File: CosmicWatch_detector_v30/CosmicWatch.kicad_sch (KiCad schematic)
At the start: 86 parts, among them J3 RJ45, P1 CONN_01X04, P10 CONN_02X02, P11 CONN_01X01, P12 CONN_01X01, P13 CONN_01X01, P14 CONN_01X01, P15 CONN_02X04, P16 CONN_01X02, P19 CONN_01X01, P2 CONN_01X01, P3 CONN_01X04, P4 CONN_01X04, P5 CONN_01X02, P7 CONN_01X01, P8 CONN_01X01, Q2 2N7002, SW1 RESET, U1 MAX5026, U13 TS5A1066, U16 UMCC, U17 UMCC, U2 SiPM_MicroFJ−300XX−TSV, U22 UMCC, U23 UMCC, U3 MMCX, U4 TS5A1066, U5 LMH6658, U5 RasberryPi_Pico, U6 LMH6658, U7 TPS6040X, U8 sd_card_socket

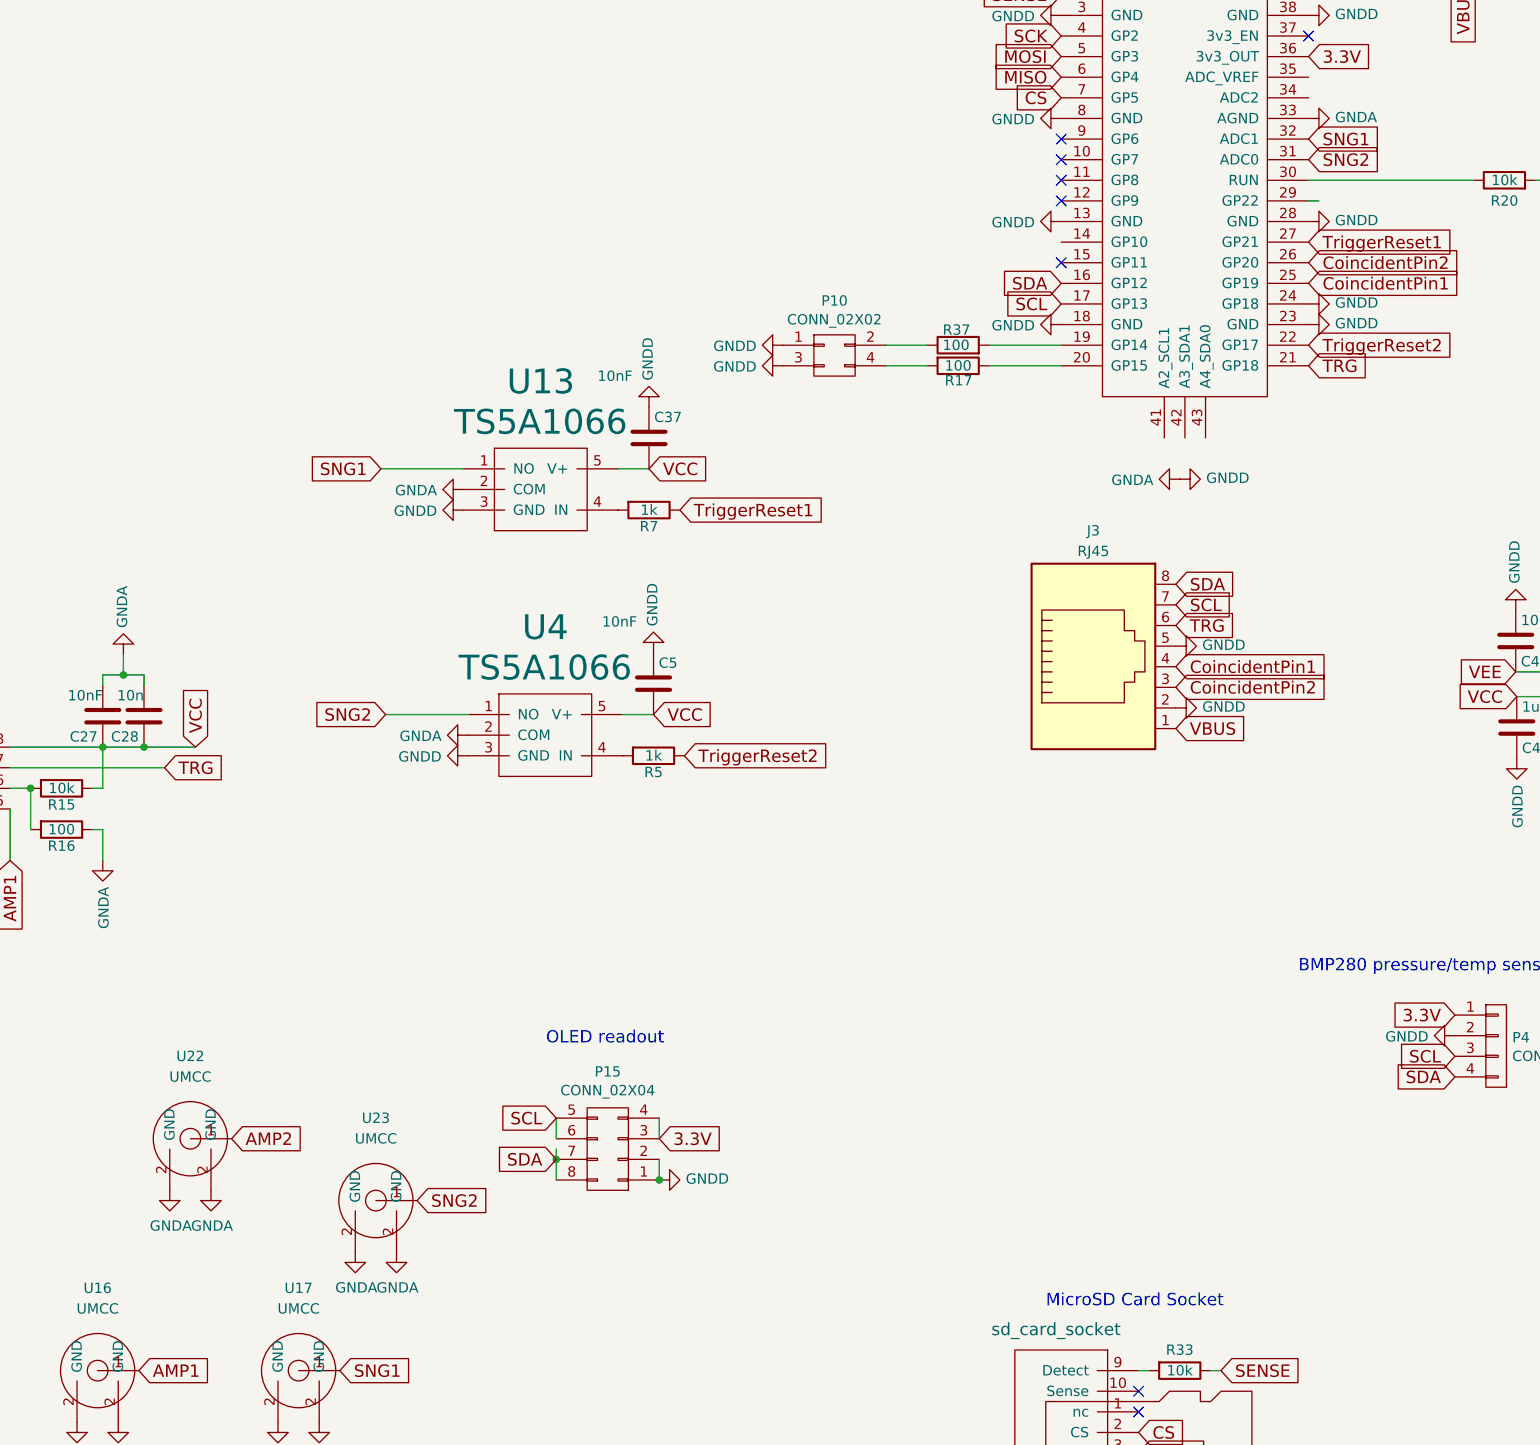
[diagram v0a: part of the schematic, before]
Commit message: updating netlist and deleting unnecessary components from PCB
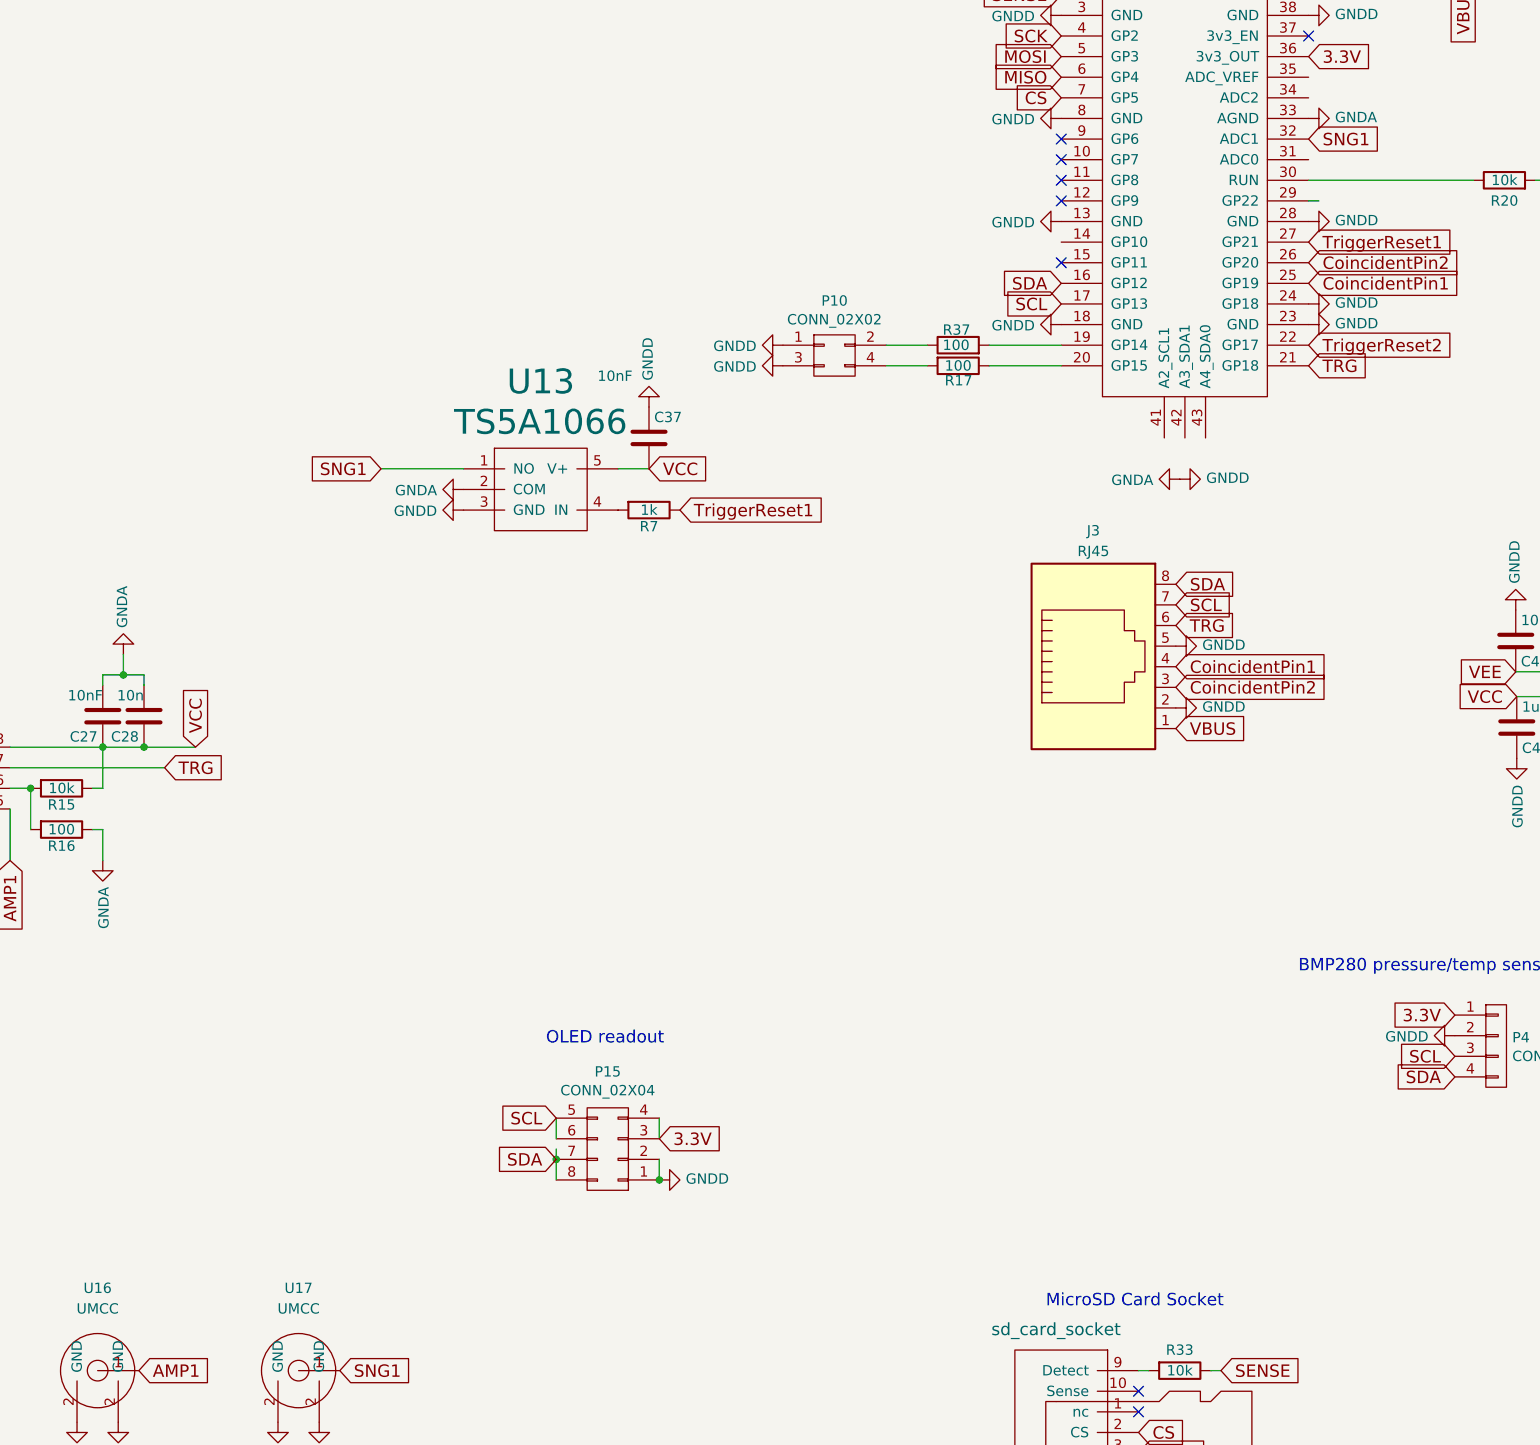
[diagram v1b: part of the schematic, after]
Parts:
- removed C5: 10nF, Capacitor_SMD:C_0603_1608Metric, symbol device:C
- removed R5: 1k, Capacitor_SMD:C_0603_1608Metric, symbol device:R
- removed U22, U23: UMCC, MyFootprints:UMCC, symbol My_Library:UMCC
- removed U4: TS5A1066, Package_TO_SOT_SMD:SOT-23-5, symbol MyLibrary:TS5A1066
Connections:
- net SNG2: no longer names the net of U5.31 (ADC0)

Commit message: updates
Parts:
- removed C37: 10nF, Capacitor_SMD:C_0603_1608Metric, symbol device:C
- removed R7: 1k, Capacitor_SMD:C_0603_1608Metric, symbol device:R
- removed U13: TS5A1066, Package_TO_SOT_SMD:SOT-23-5, symbol MyLibrary:TS5A1066
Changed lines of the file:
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@@
     (stroke (width 0) (type default))
   )
-  (wire (pts (xy 228.6 86.36) (xy 238.76 86.36))
-    (stroke (width 0) (type default))
-  )
   (wire (pts (xy 107.95 106.68) (xy 107.95 105.41))
     (stroke (width 0) (type default))
@@
     (stroke (width 0) (type default))
   )
-  (wire (pts (xy 257.81 86.36) (xy 261.62 86.36))
-    (stroke (width 0) (type default))
-  )
   (wire (pts (xy 53.34 205.74) (xy 58.42 205.74))
     (stroke (width 0) (type default))
@@
     )
   )
-  (global_label "TriggerReset1" (shape input) (at 265.43 91.44 0) (fields_autoplaced)
-    (effects (font (size 1.524 1.524)) (justify left))
-    (property "Intersheetrefs" "${INTERSHEET_REFS}" (at 283.6617 91.44 0)
-      (effects (font (size 1.27 1.27)) (justify left) hide)
-    )
-  )
   (global_label "TriggerReset2" (shape input) (at 342.9 71.12 0) (fields_autoplaced)
     (effects (font (size 1.524 1.524)) (justify left))
@@
     )
   )
-  (global_label "SNG1" (shape input) (at 228.6 86.36 180) (fields_autoplaced)
-    (effects (font (size 1.524 1.524)) (justify right))
-    (property "Intersheetrefs" "${INTERSHEET_REFS}" (at 76.2 -20.32 0)
-      (effects (font (size 1.27 1.27)) hide)
-    )
-  )
   (global_label "3.3V" (shape input) (at 321.945 210.185 0) (fields_autoplaced)
     (effects (font (size 1.524 1.524)) (justify left))
@@
     )
   )
-  (global_label "VCC" (shape input) (at 261.62 86.36 0) (fields_autoplaced)
-    (effects (font (size 1.524 1.524)) (justify left))
-    (property "Intersheetrefs" "${INTERSHEET_REFS}" (at 268.7632 86.2648 0)
-      (effects (font (size 1.524 1.524)) (justify left) hide)
-    )
-  )
   (global_label "CS" (shape input) (at 321.945 205.105 0) (fields_autoplaced)
     (effects (font (size 1.524 1.524)) (justify left))
@@
     )
   )
-  (symbol (lib_id "device:R") (at 261.62 91.44 270) (unit 1)
-    (in_bom yes) (on_board yes) (dnp no)
-    (property "Reference" "R7" (at 261.62 93.472 90)
-      (effects (font (size 1.27 1.27)))
-    )
-    (property "Value" "1k" (at 261.62 91.44 90)
-      (effects (font (size 1.27 1.27)))
-    )
-    (property "Footprint" "Capacitor_SMD:C_0603_1608Metric" (at 261.62 89.662 90)
-      (effects (font (size 1.27 1.27)) hide)
-    )
-    (property "Datasheet" "" (at 261.62 91.44 0)
-      (effects (font (size 1.27 1.27)))
-    )
-    (pin "1")
-    (pin "2")
-    (instances
-      (project "CosmicWatch"
-        (path "/4ba73f5d-b469-4168-abd4-8f6ff03fbc45"
-          (reference "R7") (unit 1)
-        )
-      )
-    )
-  )
   (symbol (lib_id "power:GNDA") (at 125.73 227.33 180) (unit 1)
     (in_bom yes) (on_board yes) (dnp no)
@@
     )
   )
-  (symbol (lib_id "power:GNDD") (at 238.76 91.44 270) (unit 1)
-    (in_bom yes) (on_board yes) (dnp no)
-    (property "Reference" "#PWR0113" (at 232.41 91.44 0)
-      (effects (font (size 1.27 1.27)) hide)
-    )
-    (property "Value" "GNDD" (at 235.5088 91.567 90)
-      (effects (font (size 1.27 1.27)) (justify right))
-    )
-    (property "Footprint" "" (at 238.76 91.44 0)
-      (effects (font (size 1.27 1.27)))
-    )
-    (property "Datasheet" "" (at 238.76 91.44 0)
-      (effects (font (size 1.27 1.27)))
-    )
-    (pin "1")
-    (instances
-      (project "CosmicWatch"
-        (path "/4ba73f5d-b469-4168-abd4-8f6ff03fbc45"
-          (reference "#PWR0113") (unit 1)
-        )
-      )
-    )
-  )
   (symbol (lib_id "conn:CONN_01X01") (at 78.74 254 90) (unit 1)
     (in_bom yes) (on_board yes) (dnp no)
@@
     )
   )
-  (symbol (lib_id "power:GNDD") (at 261.62 78.74 180) (unit 1)
-    (in_bom yes) (on_board yes) (dnp no)
-    (property "Reference" "#PWR0155" (at 261.62 72.39 0)
-      (effects (font (size 1.27 1.27)) hide)
-    )
-    (property "Value" "GNDD" (at 261.493 75.4888 90)
-      (effects (font (size 1.27 1.27)) (justify right))
-    )
-    (property "Footprint" "" (at 261.62 78.74 0)
-      (effects (font (size 1.27 1.27)))
-    )
-    (property "Datasheet" "" (at 261.62 78.74 0)
-      (effects (font (size 1.27 1.27)))
-    )
-    (pin "1")
-    (instances
-      (project "CosmicWatch"
-        (path "/4ba73f5d-b469-4168-abd4-8f6ff03fbc45"
-          (reference "#PWR0155") (unit 1)
-        )
-      )
-    )
-  )
   (symbol (lib_id "conn:CONN_01X04") (at 127 234.95 270) (unit 1)
     (in_bom yes) (on_board yes) (dnp no)
@@
         )
       )
-    )
-  )
-  (symbol (lib_id "MyLibrary:TS5A1066") (at 247.65 91.44 0) (unit 1)
-    (in_bom yes) (on_board yes) (dnp no)
-    (property "Reference" "U13" (at 248.285 75.6412 0)
-      (effects (font (size 3.048 3.048)))
-    )
-    (property "Value" "TS5A1066" (at 248.285 80.6196 0)
-      (effects (font (size 3.048 3.048)))
-    )
-    (property "Footprint" "Package_TO_SOT_SMD:SOT-23-5" (at 247.65 101.6 0)
-      (effects (font (size 3.048 3.048)) hide)
-    )
-    (property "Datasheet" "" (at 247.65 101.6 0)
-      (effects (font (size 3.048 3.048)) hide)
-    )
-    (pin "1")
-    (pin "2")
-    (pin "3")
-    (pin "4")
-    (pin "5")
-    (instances
-      (project "CosmicWatch"
-        (path "/4ba73f5d-b469-4168-abd4-8f6ff03fbc45"
-          (reference "U13") (unit 1)
-        )
-      )
-    )
-  )
-  (symbol (lib_id "device:C") (at 261.62 82.55 0) (unit 1)
-    (in_bom yes) (on_board yes) (dnp no)
-    (property "Reference" "C37" (at 262.255 80.01 0)
-      (effects (font (size 1.27 1.27)) (justify left))
-    )
-    (property "Value" "10nF" (at 255.27 74.93 0)
-      (effects (font (size 1.27 1.27)) (justify left))
-    )
-    (property "Footprint" "Capacitor_SMD:C_0603_1608Metric" (at 262.5852 86.36 0)
-      (effects (font (size 1.27 1.27)) hide)
-    )
-    (property "Datasheet" "" (at 261.62 82.55 0)
-      (effects (font (size 1.27 1.27)))
-    )
-    (pin "1")
-    (pin "2")
-    (instances
-      (project "CosmicWatch"
-        (path "/4ba73f5d-b469-4168-abd4-8f6ff03fbc45"
-          (reference "C37") (unit 1)
-        )
-      )
-    )
-  )
-  (symbol (lib_id "power:GNDA") (at 238.76 88.9 270) (unit 1)
-    (in_bom yes) (on_board yes) (dnp no)
-    (property "Reference" "#PWR0160" (at 232.41 88.9 0)
-      (effects (font (size 1.27 1.27)) hide)
-    )
-    (property "Value" "GNDA" (at 235.5088 89.027 90)
-      (effects (font (size 1.27 1.27)) (justify right))
-    )
-    (property "Footprint" "" (at 238.76 88.9 0)
-      (effects (font (size 1.27 1.27)))
-    )
-    (property "Datasheet" "" (at 238.76 88.9 0)
-      (effects (font (size 1.27 1.27)))
-    )
-    (pin "1")
-    (instances
-      (project "CosmicWatch"
-        (path "/4ba73f5d-b469-4168-abd4-8f6ff03fbc45"
-          (reference "#PWR0160") (unit 1)
-        )
-      )

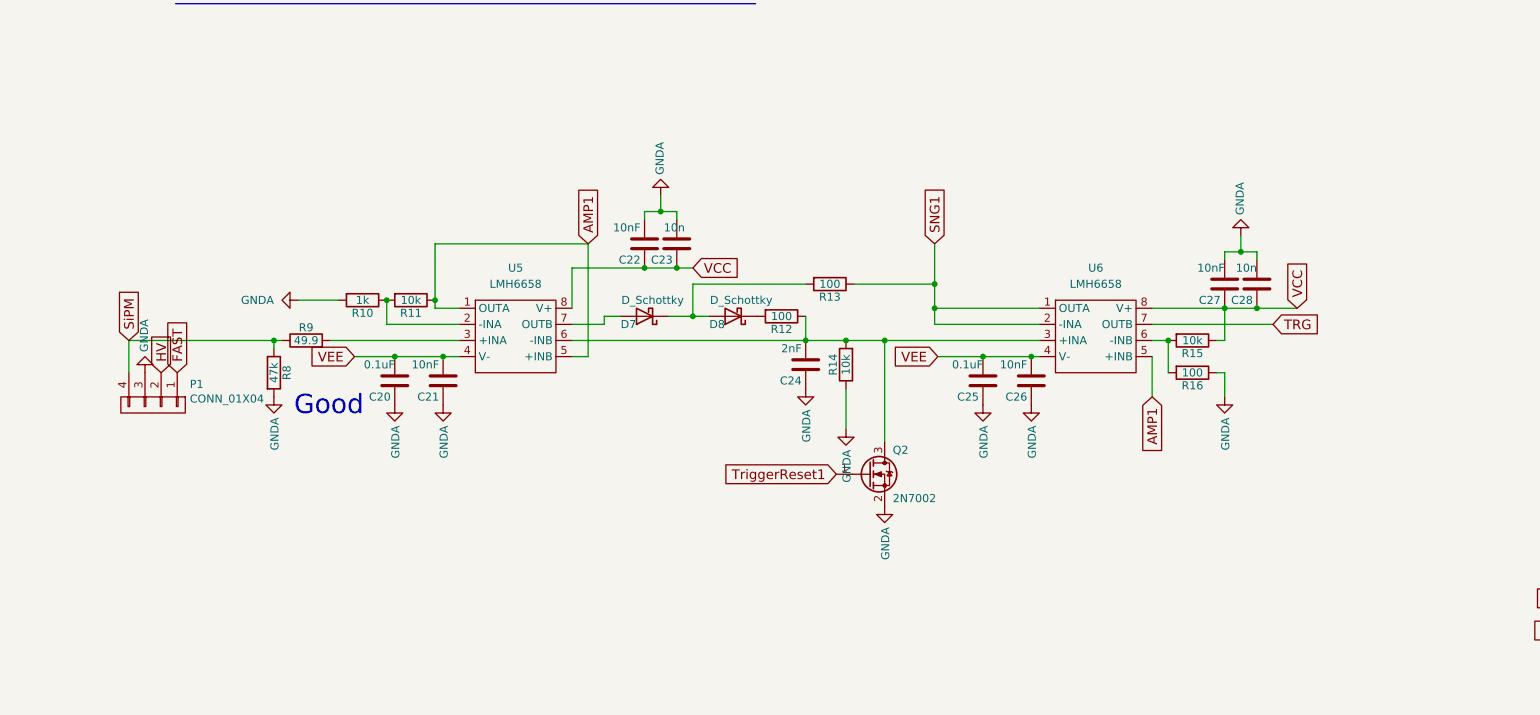
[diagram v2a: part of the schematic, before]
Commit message: added R5 on trigger reset
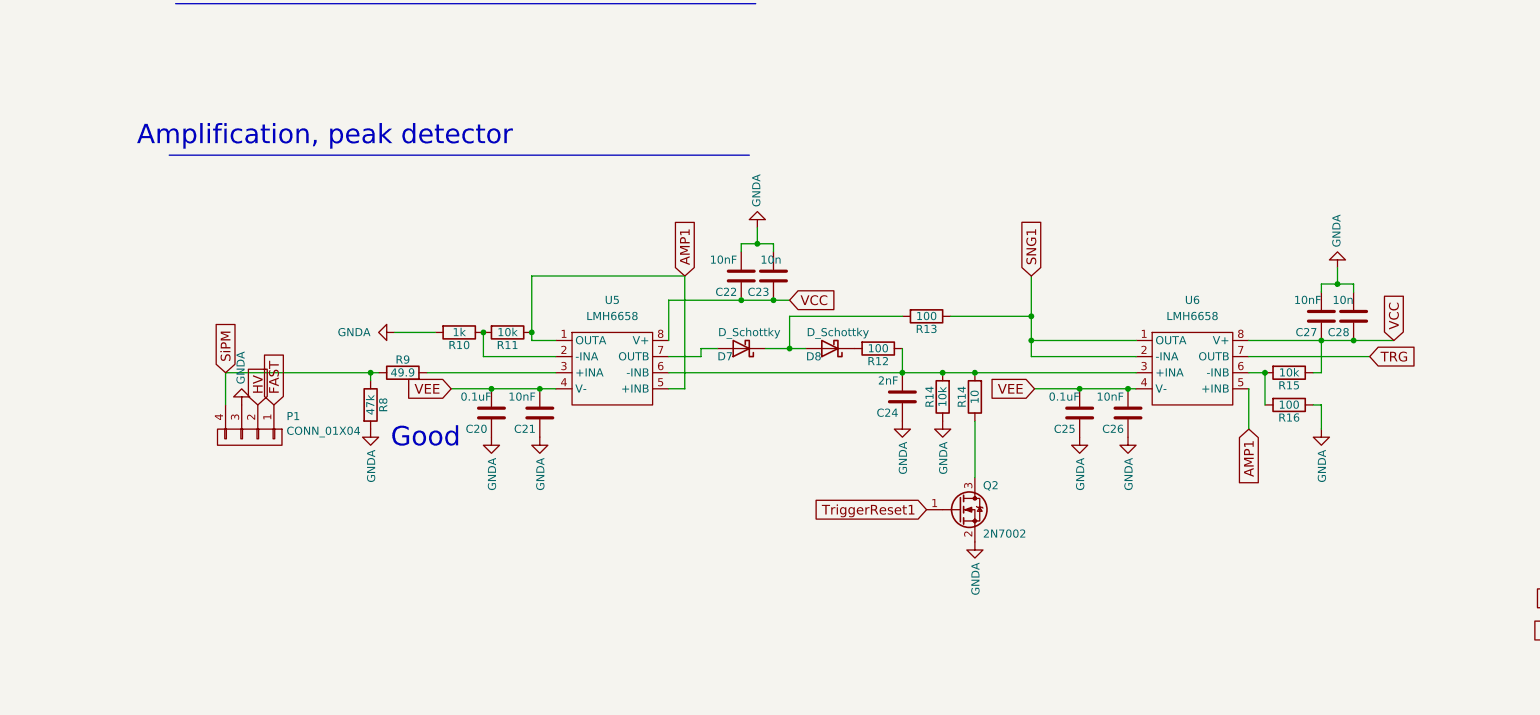
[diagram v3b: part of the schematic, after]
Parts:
- added R14: 10, Capacitor_SMD:C_0603_1608Metric, symbol device:R
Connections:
- net at C24.2, R12.1, R14.2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: now also R14.2; no longer Q2.3 (D)
- new net: Q2.3 (D), R14.1
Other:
- note added: "Amplification, peak detector"
- moved on the sheet: C20, C21, C22, C23, C24, C25, C26, C27, C28, D7, D8, P1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
